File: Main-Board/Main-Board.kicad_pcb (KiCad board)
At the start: 2 copper layers, 76.2 x 76.2 mm, 68 parts, among them J1 Power_In, J2 ESC_1, J3 ESC_2, J4 ESC_3, J5 ESC_4, J6 Receiver, J7 Aux, J8 USB_B_Micro, J9 ICSP, Q1 BSS138, Q2 BSS138, SW1 Reset, U1 MCP6001U, U2 ICM-20689, U3 FT232RL, U4 ATmega328P-AU, U5 LM1117-5.0, Y1 16 MHz

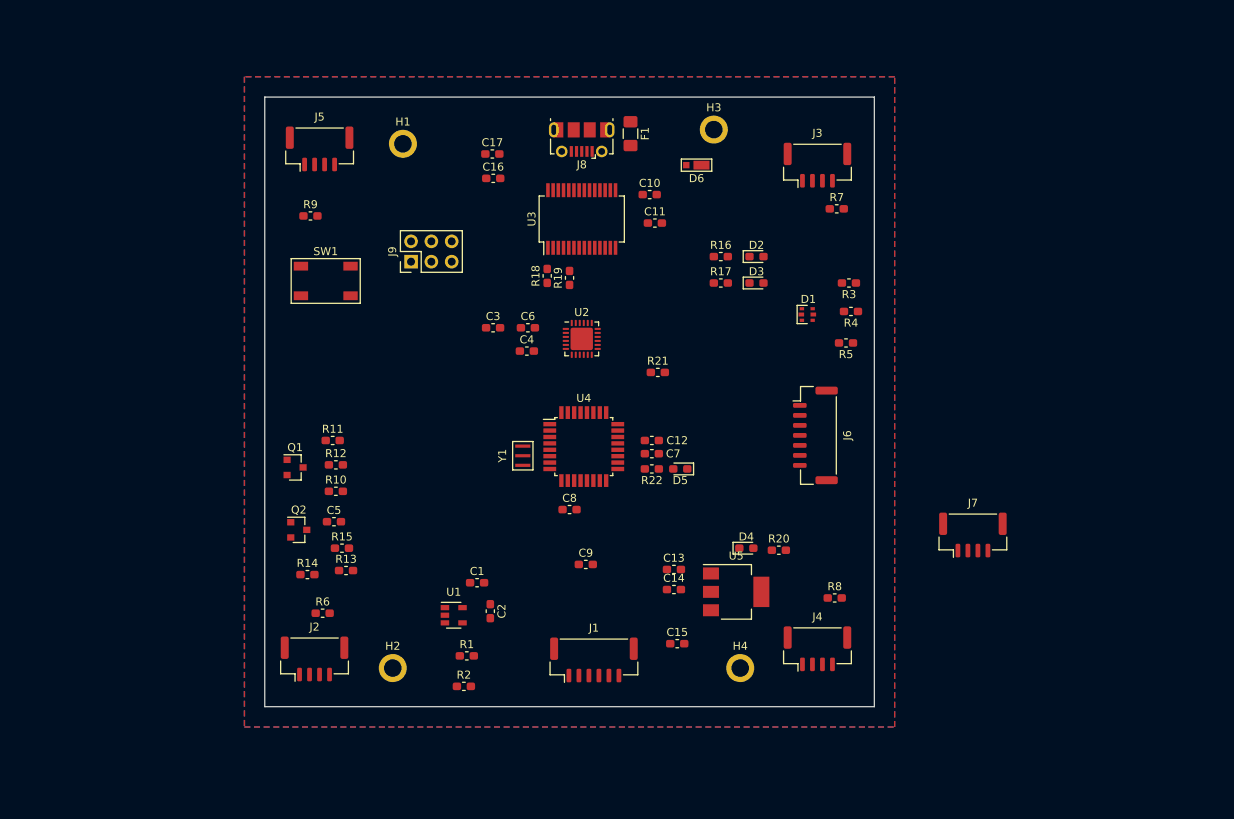
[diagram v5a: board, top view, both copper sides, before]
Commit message: Routed IMU
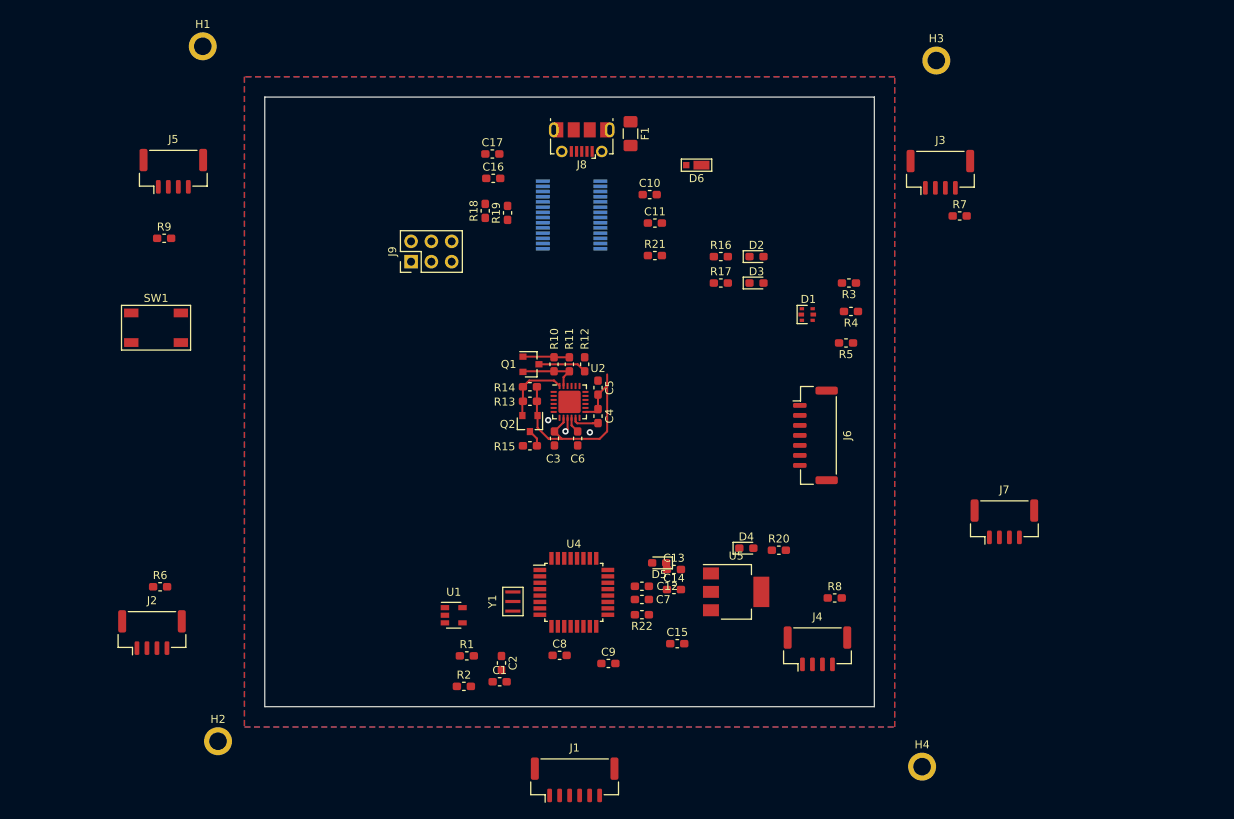
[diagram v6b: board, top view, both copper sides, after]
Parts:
- U3: moved to B.Cu
- moved C5 37.0 mm to (92.5, 112.5), turned to 270 degrees
- moved R14 36.4 mm to (83.9, 112.4)
- moved R12 33.5 mm to (90.8, 109.6), turned to 90 degrees
- moved Q1 32.2 mm to (84.1, 109.6)
- moved Q2 31.8 mm to (83.9, 117.0), turned to 270 degrees
- moved R10 31.6 mm to (87.0, 109.6), turned to 90 degrees
- moved R13 31.2 mm to (83.9, 114.2)
- moved R11 31.1 mm to (88.9, 109.6), turned to 90 degrees
- moved H3 29.1 mm to (134.7, 71.6)
- moved H1 27.8 mm to (43.1, 69.8)
- moved R15 26.8 mm to (83.9, 119.8), turned to 180 degrees
- moved H4 25.9 mm to (133.0, 159.9)
- moved H2 23.7 mm to (45.0, 156.7)
- moved SW1 22.0 mm to (37.2, 105.0)
- moved J2 20.6 mm to (36.7, 143.1)
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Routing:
- net +3V3: track 0.00 -> 36.4 mm
- net IMU_SDA_LL: track 0.00 -> 8.81 mm
- net IMU_SCL_LL: track 0.00 -> 7.97 mm
- net A5_SCL: track 0.00 -> 6.08 mm
- net GND: track 0.00 -> 5.19 mm, vias 0 -> 3
- net A4_SDA: track 0.00 -> 2.15 mm
- net Net-(C6-Pad1): track 0.00 -> 2.03 mm
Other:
- net class Default: clearance 0.2 -> 0.1778; trace_width 0.25 -> 0.254
- rule solder_mask_min_width: 0.25 -> 0.254
- rule trace_clearance: 0.2 -> 0.1778

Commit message: Shrunk board to approx 65 mm and layed out approx positions
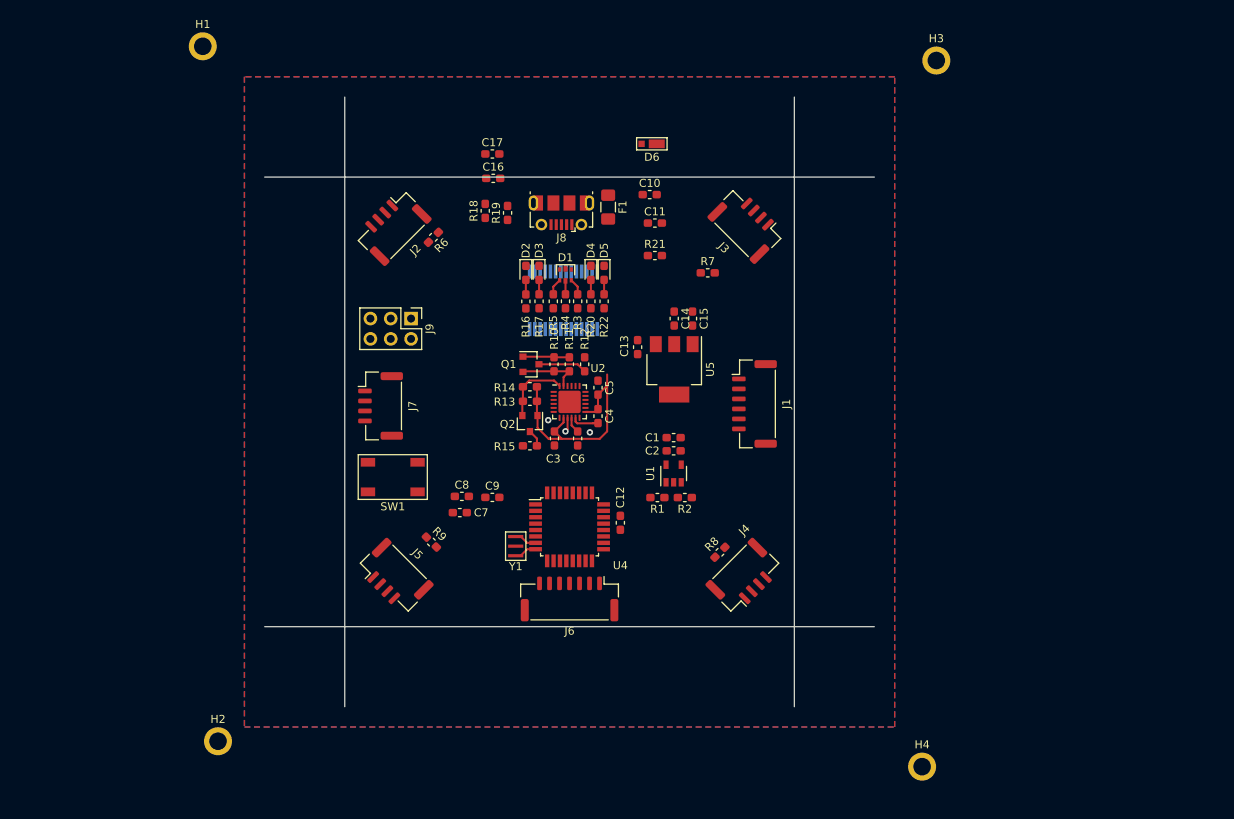
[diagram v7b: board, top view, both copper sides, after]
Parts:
- moved J7 79.3 mm to (65.3, 114.8), turned to 270 degrees
- moved J2 58.9 mm to (66.8, 92.5), turned to 225 degrees
- moved J5 57.7 mm to (67.1, 136.1), turned to 315 degrees
- moved R6 55.5 mm to (71.9, 93.7), turned to 225 degrees
- moved J1 52.1 mm to (112.0, 114.6), turned to 270 degrees
- moved R9 50.6 mm to (71.6, 131.8), turned to 315 degrees
- moved C15 40.7 mm to (104.3, 103.9), turned to 270 degrees
- moved D4 39.5 mm to (91.6, 98.2), turned to 270 degrees
- moved R22 39.5 mm to (93.2, 101.7), turned to 270 degrees
- moved R20 39.0 mm to (91.6, 101.7), turned to 270 degrees
- moved C1 37.5 mm to (101.9, 118.8), turned to 180 degrees
- moved R5 37.0 mm to (86.9, 101.7), turned to 90 degrees
- moved J6 36.9 mm to (88.9, 138.9), turned to 180 degrees
- moved D5 36.9 mm to (93.2, 98.2), turned to 270 degrees
- moved R2 36.3 mm to (103.3, 126.3), turned to 180 degrees
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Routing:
- net Net-(U4-Pad8): track 0.00 -> 2.82 mm
- net Net-(U4-Pad7): track 0.00 -> 2.81 mm
- net Net-(D1-Pad5): track 0.00 -> 2.08 mm
- net Net-(D1-Pad1): track 0.00 -> 2.08 mm
- net Net-(D2-Pad2): track 0.00 -> 1.82 mm
- net Net-(D5-Pad2): track 0.00 -> 1.81 mm
- net Net-(D4-Pad2): track 0.00 -> 1.81 mm
- net Net-(D3-Pad2): track 0.00 -> 1.81 mm
- net Net-(D1-Pad3): track 0.00 -> 1.68 mm
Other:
- outline, holes or cut-outs redrawn

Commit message: Dimensions 50 mm x 50 mm with 45 mm c-c holes. ESC connectors placed
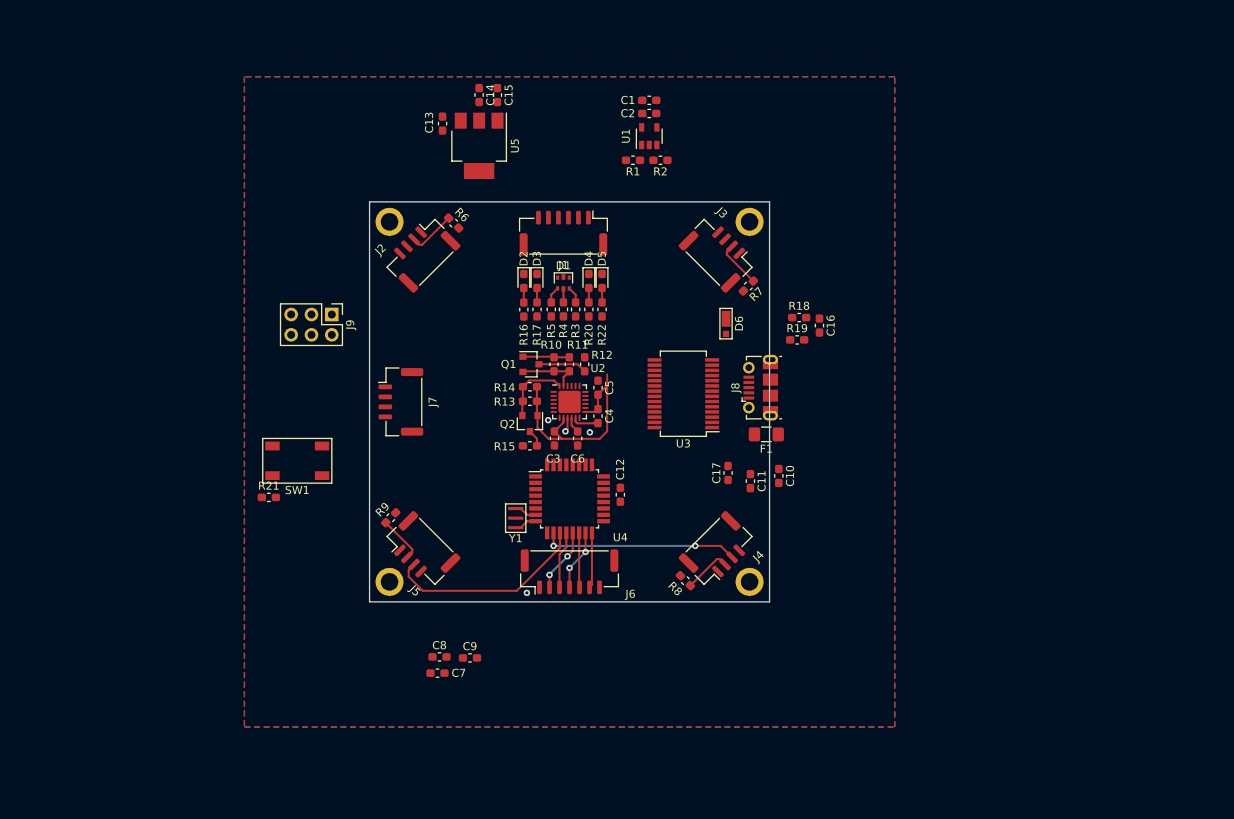
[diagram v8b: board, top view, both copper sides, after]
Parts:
- U3: moved to F.Cu
- moved R21 56.9 mm to (51.3, 126.2)
- moved C17 49.6 mm to (108.7, 123.2), turned to 90 degrees
- moved C16 44.7 mm to (120.1, 104.8), turned to 270 degrees
- moved C1 42.3 mm to (98.9, 76.6)
- moved C2 42.3 mm to (98.9, 78.3)
- moved R1 42.3 mm to (96.8, 84.1)
- moved R2 42.3 mm to (100.3, 84.1)
- moved U1 42.3 mm to (98.9, 81.1)
- moved R18 41.4 mm to (117.6, 103.8), turned to 0 degrees
- moved R19 39.5 mm to (117.3, 106.6), turned to 0 degrees
- moved C10 38.7 mm to (115.1, 123.6), turned to 270 degrees
- moved C13 37.1 mm to (73.0, 79.5)
- moved C14 37.1 mm to (77.6, 75.9)
- moved C15 37.1 mm to (79.9, 75.9)
- moved U5 37.1 mm to (77.6, 82.3)
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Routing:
- net D7: track 0.00 -> 25.5 mm
- net D6: track 0.00 -> 24.6 mm, vias 0 -> 2
- net D9: track 0.00 -> 8.02 mm, vias 0 -> 2
- net D11: track 0.00 -> 7.64 mm, vias 0 -> 2
- net D8: track 0.00 -> 7.17 mm
- net D12: track 0.00 -> 6.94 mm
- net D10: track 0.00 -> 6.84 mm
- net Net-(J4-Pad2): track 0.00 -> 6.00 mm
- net Net-(J5-Pad2): track 0.00 -> 6.00 mm
- net Net-(J2-Pad2): track 0.00 -> 6.00 mm
- net Net-(J3-Pad2): track 0.00 -> 5.99 mm
- net GND: vias 3 -> 4
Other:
- board size 76.2 x 76.2 mm -> 50 x 50 mm
